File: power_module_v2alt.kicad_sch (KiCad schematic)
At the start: 0 parts

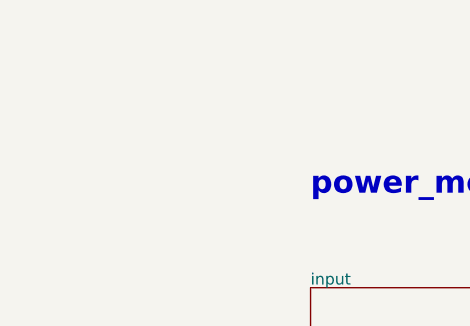
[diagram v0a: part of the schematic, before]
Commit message: DFN-8 pad rename fixes Q sync + META1 singleton for placer power nets
Two fixes uncovered while diagnosing the placement pass:

DFN-8 pad rename (fixes 6× MOSFET floating pads)

The AON7544 MOSFETs' schematic symbol is Device:Q_NMOS which uses G/D/S
pin identifiers, but the DFN-8_L3.3-W3.3-P0.65-BL-2 footprint uses
numeric 1..5.  sync_schematic_to_board couldn't match the pin names, so
all 30 pads across the 6 FETs (Q1_BMS1, Q2_BMS1, Q1..Q4_BUCKBOOST1) were
sitting with net=UNASSIGNED — the FETs were electrically floating on the
board and every gate/drain/source route was going nowhere.

Renamed the footprint pads to match the symbol pin names:
  pad "1" → "S"    (was Source #1)
  pad "2" → "S"    (Source #2)
  pad "3" → "S"    (Source #3)
  pad "4" → "G"    (Gate)
  pad "5" → "D"    (Drain, unified custom pad)

Renamed the corresponding pads in the existing PCB Q footprints too so
re-sync picks them up without a wipe.  After sync: Q1_BMS1 pads assigned
D→MID, G→Q1_G, S→VSS (×3).  Net-assigned pad count: 245 → 275 (+30).

Alternative — swap Q_NMOS → power_module_lib:AON7544 symbol (which
already has correct 1..5 pinout) — is more thorough but requires
rebuilding all 6 FET wirings.  Deferred.

META1 singleton with mcp_spring_classes

Authored the project's Schematic_Metadata singleton with:
  mcp_constraint_version = 2
  mcp_spring_classes = {"nets": {"BAT+": "PLANE", "VBUS_9V": "PLANE",
                                  "VBUS_RAW": "PLANE", "VOUT_12V":
                                  "PLANE", "VSYS": "PLANE"}}

These are the multi-node cross-group power rails the earlier
relax_placement pass was pulling components across.  With them classified
PLANE, the placer's spring engine will skip attraction on those edges
(they route via copper pours anyway, so no useful "pull toward
neighbour" signal).  Next relax pass should keep Q1..Q4 near LM5176
instead of getting dragged out by BAT+/VOUT_12V drain edges.

Depends on KiCAD-MCP-Server develop (uncommitted): the
`_find_l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
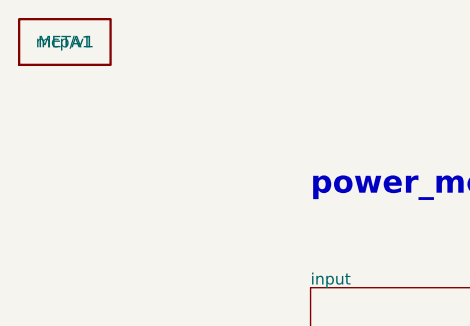
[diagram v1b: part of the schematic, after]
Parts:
- added META1: mcp/v1, symbol mcp_meta:Schematic_Metadata
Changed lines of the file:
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@@
     (path "/" (page "1"))
   )
+	(symbol
+		(lib_id "mcp_meta:Schematic_Metadata")
+		(at 12.7 12.7 0)
+		(unit 1)
+		(exclude_from_sim yes)
+		(in_bom no)
+		(on_board no)
+		(dnp no)
+		(property "Reference" "META1"
+			(at 12.7 12.7 0)
+			(effects
+				(font
+					(size 1.27 1.27)
+				)
+			)
+		)
+		(property "Value" "mcp/v1"
+			(at 12.7 12.7 0)
+			(effects
+				(font
+					(size 1.27 1.27)
+				)
+			)
+		)
+		(property "Footprint" ""
+			(at 12.7 12.7 0)
+			(effects
+				(font
+					(size 1.27 1.27)
+				)
+				(hide yes)
+			)
+		)
+		(property "Datasheet" ""
+			(at 12.7 12.7 0)
+			(effects
+				(font
+					(size 1.27 1.27)
+				)
+				(hide yes)
+			)
+		)
+		(property "Description" "Project-wide MCP metadata (singleton)."
+			(at 12.7 12.7 0)
+			(effects
+				(font
+					(size 1.27 1.27)
+				)
+				(hide yes)
+			)
+		)
+		(property "Schematic_Metadata_Marker" "mcp/v1"
+			(at 12.7 12.7 0)
+			(effects
+				(font
+					(size 1.27 1.27)
+				)
+				(hide yes)
+			)
+		)
+		(property "mcp_constraint_version" "2"
+			(at 12.7 12.7 0)
+			(effects
+				(font
+					(size 1.27 1.27)
+				)
+				(hide yes)
+			)
+		)
+		(property "mcp_spring_classes" "{\"nets\":{\"BAT+\":\"PLANE\",\"VBUS_9V\":\"PLANE\",\"VBUS_RAW\":\"PLANE\",\"VOUT_12V\":\"PLANE\",\"VSYS\":\"PLANE\"}}"
+			(at 12.7 12.7 0)
+			(effects
+				(font
+					(size 1.27 1.27)
+				)
+				(hide yes)
+			)
+		)
+		(instances
+			(project "power_module_v2alt"
+				(path "/b266f3b8-db6b-493d-8968-5af48ab0203e"
+					(reference "META1")
+					(unit 1)
+				)
+			)
+		)
+	)
 )

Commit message: Step 5: pre-route audit + same-net zones + plane pours
Netclasses + patterns
- POWER_5A (1.65 mm track, 0.8/0.4 via) — BAT+, VOUT_12V
- POWER_2A (0.60 mm track, 0.6/0.3 via) — VBUS_RAW, VBUS_9V, VSYS
- mcp_expected_netclass_patterns authored on META1 singleton for
  drift protection.

Stale-net merges (sync_schematic_to_board leftovers)
- Net-(C6_BUCKBOOST1-Pad2) → SW2  (6 pads incl. Q4.S ×3, L1.pad2)
- Net-(U1_BMS1-Pad6)       → TS1  (BQ76920.6, R8.2, TH1.1)
These were both labelled correctly in the schematic; the PCB had
stale auto-names from an earlier state that later syncs never
migrated.  Same class of bug as the EN cross-sheet issue —
sync_schematic_to_board doesn't fully update net names once a net is
created.  Merged in .kicad_pcb via search-and-repoint script; net
numbering preserved so no downstream references break.

pin_zone_same_net (22 applied, 6 rejected)
- Q1..Q4 FET Source triplets (VSS / GND / SW1 / SW2)
- BQ76920 BAT+ pin pair (9+10)
- LM5176 EP thermal pad (pin 29) — 34.9 mm² GND cluster on B.Cu
- IP2326 VSYS pin pair (19+20) and BAT+ pin pair (21+22)
- USB-C shield pads (S1 pair)
- Rejections all valid (would overlap foreign pads on connectors
  and the LM5176 body).

Plane pours
- In1.Cu = GND across full board outline (0.5 mm inset)
- In2.Cu = BAT+ across full board outline
- VOUT_12V will route as short traces on F.Cu/B.Cu from LM5176's
  output pins to the C10/C11 output caps — the net is local and
  doesn't need its own plane.

pre_route_audit: 66 → 7 unreachable spokes after pours
- 5 LM5176 comp-loop signals (FB / RT / COMP / SLOPE / SS) that
  the audit can't route at netclass width because the LM5176 body
  blocks the direct F.Cu path; freerouting will handle with short
  hops.
- 2 BAT+ BAT1.1 → IP2326.21/22: spoke_no_anchor is a tool artifact
  for BAT1's large custom B.Cu pads (the audit can't find a
  representative anchor point on a 41×18 mm pad).  In practice the
  BAT+ plane on In2.Cu will thermal-connect BAT1 to the charger via
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
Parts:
- META1: mcp_expected_netclass_patterns (none) -> [{"netclass":"POWER_5A","pattern":"BAT+"},{"netclass":"POWE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
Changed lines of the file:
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@@
+			)
+		)
+		(property "mcp_expected_netclass_patterns" "[{\"netclass\":\"POWER_5A\",\"pattern\":\"BAT+\"},{\"netclass\":\"POWER_5A\",\"pattern\":\"VOUT_12V\"},{\"netclass\":\"POWER_2A\",\"pattern\":\"VBUS_RAW\"},{\"netclass\":\"POWER_2A\",\"pattern\":\"VBUS_9V\"},{\"netclass\":\"POWER_2A\",\"pattern\":\"VSYS\"}]"
+			(at 12.7 12.7 0)
+			(effects
+				(font
+					(size 1.27 1.27)
+				)
+				(hide yes)
 			)
 		)

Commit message: netclass: add BAT-, CELL1_TOP, CELL2_TOP to POWER_5A (1.65 mm cell-tap traces)
Series 3S1P pack: cell taps CELL1_TOP and CELL2_TOP carry the same
5A continuous / 6.5A peak current as BAT+ and BAT-.  Previously only
BAT+ and VOUT_12V were on POWER_5A; the cell taps and BAT- fell to
Default (0.2 mm) and would have been auto-routed as thin signal traces.

Sizing per IPC-2221 external, 1oz copper, 10°C rise at 5A → 1.65 mm.

Also update mcp_expected_netclass_patterns on META1 singleton so the
drift check covers all 8 patterns.  verify_netclass_patterns: 8/8
present, no drift.

Next autoroute pass will pick the wider width for the cell-tap ratlines.

Co-Authored-By: Claude Opus 4.7 <noreply@anthropic.com>
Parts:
- META1: mcp_expected_netclass_patterns [{"netclass":"POWER_5A","pattern":"BAT+"},{"netclass":"POWER_5A","pattern":"VOUT_12V"},{"netclass":"POWER_2A","pattern":"VBUS_RAW"},{"netclass":"POWER_2A","pattern":"VBUS_9V"},{"netclass":"POWER_2A","pattern":"VSYS"}] -> [{"netclass":"POWER_5A","pattern":"BAT+"},{"netclass":"POWER_5A","pattern":"BAT-"},{"netclass":"POWER_5A","pattern":"CELL1_TOP"},{"netclass":"POWER_5A","pattern":"CELL2_TOP"},{"netclass":"POWER_5A","pattern":"VOUT_12V"},{"netclass":"POWER_2A","pattern":"VBUS_RAW"},{"netclass":"POWER_2A","pattern":"VBUS_9V"},{"netclass":"POWER_2A","pattern":"VSYS"}]
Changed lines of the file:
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@@
 			)
 		)
-		(property "mcp_expected_netclass_patterns" "[{\"netclass\":\"POWER_5A\",\"pattern\":\"BAT+\"},{\"netclass\":\"POWER_5A\",\"pattern\":\"VOUT_12V\"},{\"netclass\":\"POWER_2A\",\"pattern\":\"VBUS_RAW\"},{\"netclass\":\"POWER_2A\",\"pattern\":\"VBUS_9V\"},{\"netclass\":\"POWER_2A\",\"pattern\":\"VSYS\"}]"
+		(property "mcp_expected_netclass_patterns" "[{\"netclass\":\"POWER_5A\",\"pattern\":\"BAT+\"},{\"netclass\":\"POWER_5A\",\"pattern\":\"BAT-\"},{\"netclass\":\"POWER_5A\",\"pattern\":\"CELL1_TOP\"},{\"netclass\":\"POWER_5A\",\"pattern\":\"CELL2_TOP\"},{\"netclass\":\"POWER_5A\",\"pattern\":\"VOUT_12V\"},{\"netclass\":\"POWER_2A\",\"pattern\":\"VBUS_RAW\"},{\"netclass\":\"POWER_2A\",\"pattern\":\"VBUS_9V\"},{\"netclass\":\"POWER_2A\",\"pattern\":\"VSYS\"}]"
 			(at 12.7 12.7 0)
 			(effects
